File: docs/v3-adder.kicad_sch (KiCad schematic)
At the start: 101 parts, among them J1 Thonkiconn, J2 Thonkiconn, J3 Thonkiconn, J4 Thonkiconn, J5 Thonkiconn, J6 Thonkiconn, J7 Thonkiconn, J8 Thonkiconn, P1 Eurorack 2x5, SW1A SUBMINI ON-OFF-ON, SW1B SUBMINI ON-ON, SW2A SUBMINI ON-OFF-ON, SW2B SUBMINI ON-ON-ON, SW3A SUBMINI ON-OFF-ON, SW3B SUBMINI ON-ON-ON, SW4A SUBMINI ON-OFF-ON, SW4B SUBMINI ON-ON-ON, U1 OPA4196, U2 OPA4196, U3 OPA4196, U4 L78L05, U5 L79L05

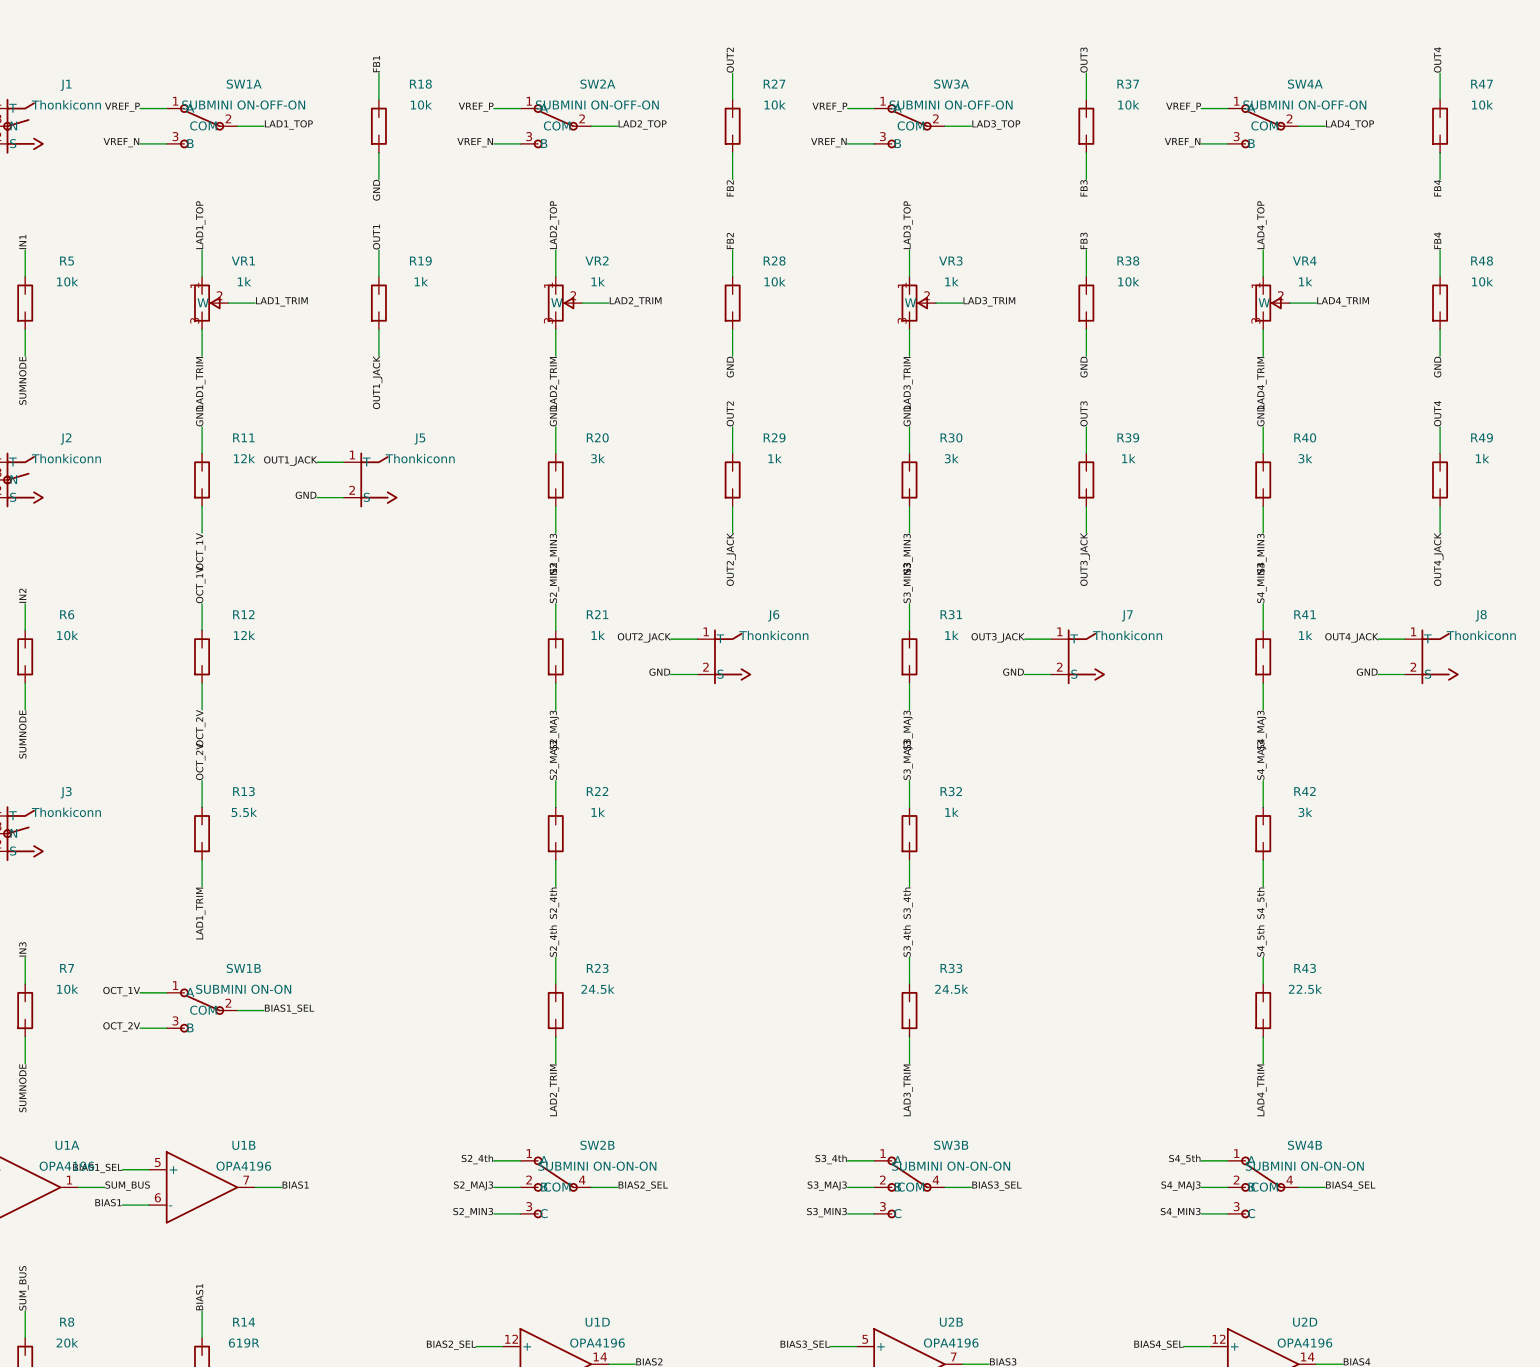
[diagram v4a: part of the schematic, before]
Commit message: Schematic: wire the real Taiway switches, cross-check against the panel
Part is Taiway 200-MDP6-T1B1M2QE. Datasheet fetched and read: series 200
subminiature, pins 1-2-3 pole A with 2 common, 4-5-6 pole B with 5 common,
B1 bushing 10-48 UNS Ø4.80 with a recommended Ø4.95 panel hole - so the panel's
Ø5.0 holes are right, though it does not cut the optional 4.55 anti-rotation
flat.

The selector was drawn as an ideal 4-pin 1P3T, which no such part is. It is now
a real 6-pin DPDT with the poles cascaded: pole A's common is the output, one
of its throws is a tap outright, the other feeds pole B's common, and pole B
picks between the remaining two. Tying the commons instead would short two
ladder taps in every position.

MDP-6 is not in Taiway's catalogue - the sheet documents MDP-1..MDP-5 and says
custom configurations are by request - so its contact sequence is unpublished
and two are possible. ONONON_VARIANT selects between them, defaulting to 1,
with the meter check documented. It changes only which of pins 1/3 carries a
tap and which links to pole B.

Wiring the switch properly exposed a cross-artifact bug: the schematic put the
4th on the up throw while the panel silkscreens MAJ there. That would have
shipped a module whose front lied about its own switches. Throws are now named
explicitly rather than positionally, and check_panel_agreement() imports the
panel generator and asserts that every printed label matches the tap it wires,
and that each group drives the output it claims. Verified against a swap.

BOM now carries real part numbers: 4x 200-MSP3 polarity, 1x 200-MSP1 octave
magnitude, 3x 200-MDP6 quality.

ERC still 0 errors, 23 footprint warnings on the custom parts.

Co-Authored-By: Claude Opus 5 <noreply@anthropic.com>
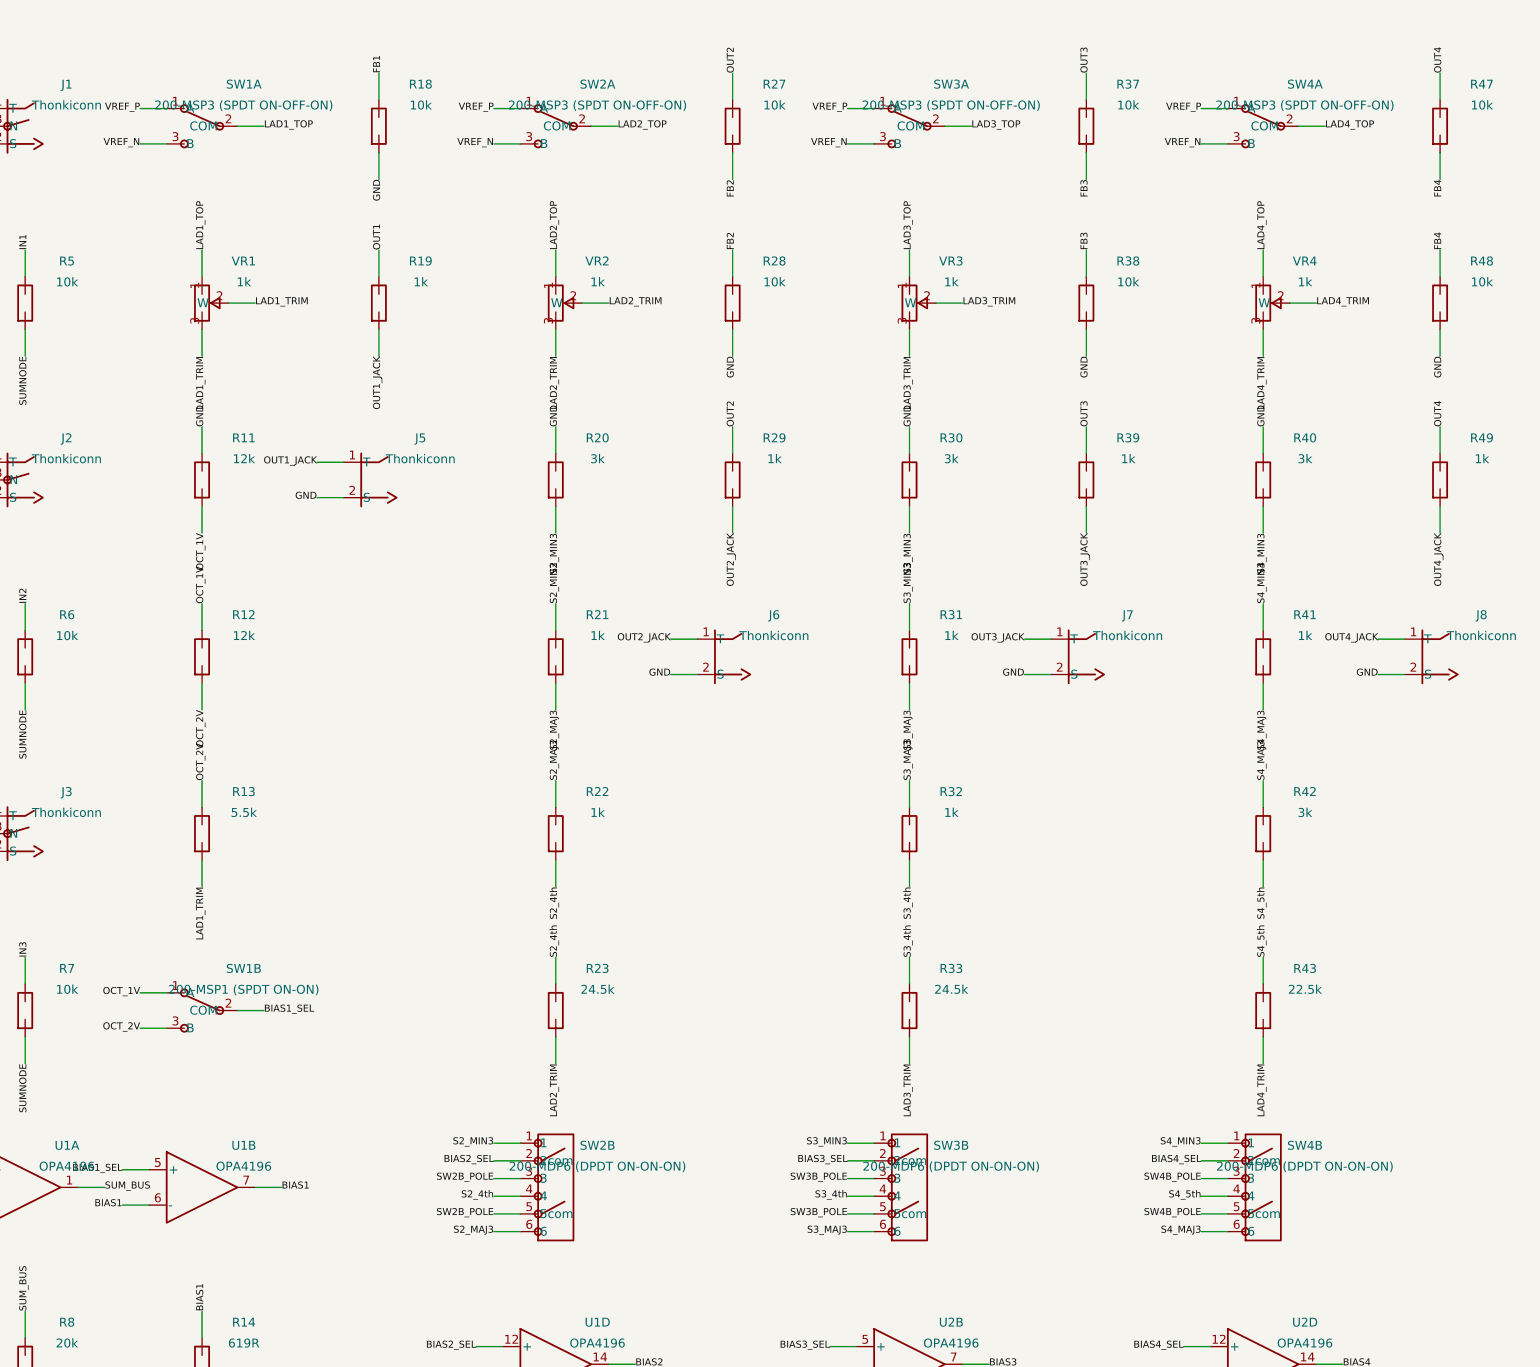
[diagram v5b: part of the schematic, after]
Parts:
- removed C20: 330pF, Capacitor_SMD:C_0805_2012Metric, symbol adder:C
- removed R44: 619R, Resistor_SMD:R_0805_2012Metric, symbol adder:R
- removed R47, R48: 10k, Resistor_SMD:R_0805_2012Metric, symbol adder:R
- removed SW3A, SW4A: SUBMINI ON-OFF-ON, SUBMINI_TOGGLE, symbol adder:SW_ONOFFON
- removed SW3B, SW4B: SUBMINI ON-ON-ON, SUBMINI_TOGGLE, symbol adder:SW_1P3T
- removed unit 2 of U2
- removed unit 3 of U2
- added J8: Thonkiconn, THONKICONN-TIGHT, symbol adder:JACK
- added R34: 619R, Resistor_SMD:R_0805_2012Metric, symbol adder:R
- added R37, R46: 10k, Resistor_SMD:R_0805_2012Metric, symbol adder:R
- added R40: 3k, Resistor_SMD:R_0805_2012Metric, symbol adder:R
- added R49: 1k, Resistor_SMD:R_0805_2012Metric, symbol adder:R
- added SW3A: 200-MSP3 (SPDT ON-OFF-ON), TAIWAY_200_SP_M2, symbol adder:SW_ONON
- added SW3B, SW4B: 200-MDP6 (DPDT ON-ON-ON), TAIWAY_200_DP_M2, symbol adder:SW_DPDT
- added unit 1 of U3
- C20: renamed from R46; value 10k -> 330pF; footprint Resistor_SMD:R_0805_2012Metric -> Capacitor_SMD:C_0805_2012Metric; symbol adder:R -> adder:C
- R44: renamed from R45; value 10k -> 619R
- R45: renamed from U3; value OPA4196 -> 10k; footprint Package_SO:SOIC-14_3.9x8.7mm_P1.27mm -> Resistor_SMD:R_0805_2012Metric; symbol adder:OPA4196 -> adder:R
- R47: renamed from R49; value 1k -> 10k
- R48: renamed from J8; value Thonkiconn -> 10k; footprint THONKICONN-TIGHT -> Resistor_SMD:R_0805_2012Metric; symbol adder:JACK -> adder:R
- SW1A, SW2A: value SUBMINI ON-OFF-ON -> 200-MSP3 (SPDT ON-OFF-ON); footprint SUBMINI_TOGGLE -> TAIWAY_200_SP_M2; symbol adder:SW_ONOFFON -> adder:SW_ONON
- SW1B: value SUBMINI ON-ON -> 200-MSP1 (SPDT ON-ON); footprint SUBMINI_TOGGLE -> TAIWAY_200_SP_M2; symbol adder:SW_ONOFFON -> adder:SW_ONON
- SW2B: value SUBMINI ON-ON-ON -> 200-MDP6 (DPDT ON-ON-ON); footprint SUBMINI_TOGGLE -> TAIWAY_200_DP_M2; symbol adder:SW_1P3T -> adder:SW_DPDT
- SW4A: renamed from VR4; value 1k -> 200-MSP3 (SPDT ON-OFF-ON); footprint PV36W-MULTITURN-TRIMMER -> TAIWAY_200_SP_M2; symbol adder:POT -> adder:SW_ONON
- U2: renamed from R34; value 619R -> OPA4196; footprint Resistor_SMD:R_0805_2012Metric -> Package_SO:SOIC-14_3.9x8.7mm_P1.27mm; symbol adder:R -> adder:OPA4196
- U2: renamed from R37; value 10k -> OPA4196; footprint Resistor_SMD:R_0805_2012Metric -> Package_SO:SOIC-14_3.9x8.7mm_P1.27mm; symbol adder:R -> adder:OPA4196
- VR4: renamed from R40; value 3k -> 1k; footprint Resistor_SMD:R_0805_2012Metric -> PV36W-MULTITURN-TRIMMER; symbol adder:R -> adder:POT
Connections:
- net BIAS2_SEL: now also SW2B.2 (2com); no longer SW2B.4 (COM)
- net BIAS3: now also U2.6 (-), U2.7, R34.1; no longer U2.1
- net BIAS3_SEL: now also U2.5 (+), SW3B.2 (2com)
- net BIAS3_SNUB: now also R34.2; no longer U2.2
- net BIAS4: now also R44.1, R46.1; no longer C20.1
- net BIAS4_SEL: now also SW4B.2 (2com)
- net BIAS4_SNUB: now also C20.1, R44.2
- net FB3: now also U2.9 (-), R37.2; no longer U2.2
- net FB4: now also R47.2, R48.1, U3.2 (-); no longer R45.2 (-)
- net GND: now also C20.2, J8.2 (S), R40.1; no longer VR4.1
- net LAD3_TOP: now also SW3A.2 (COM)
- net LAD4_TOP: now also SW4A.2 (COM), VR4.1; no longer SW4A.1
- net LAD4_TRIM: now also VR4.2 (W), VR4.3; no longer SW4A.2 (W), SW4A.3
- net OUT3: now also R45.1, U2.8, R37.1; no longer R44.1, U2.1
- net OUT4: now also R49.1, U3.1; no longer R45.1
- net OUT4_JACK: now also J8.1 (T), R49.2; no longer R47.2, R48.1 (T)
- net S2_4th: now also SW2B.4; no longer SW2B.1 (A)
- net S2_MAJ3: now also SW2B.6; no longer SW2B.2 (B)
- net S2_MIN3: now also SW2B.1; no longer SW2B.3 (C)
- net S3_4th: now also SW3B.4
- net S3_MAJ3: now also SW3B.6
- net S3_MIN3: now also SW3B.1
- net S4_5th: now also SW4B.4
- net S4_MAJ3: now also SW4B.6
- net S4_MIN3: now also R40.2, SW4B.1; no longer VR4.2
- net SUM3: now also U2.10 (+)
- net SUM4: now also R45.2, R46.2, U3.3 (+); no longer C20.2, R44.2, R45.3 (+)
- net VREF_N: now also SW4A.3 (B), SW3A.3 (B)
- net VREF_P: now also SW4A.1 (A), SW3A.1 (A)
- new net SW2B_POLE: SW2B.3, SW2B.5 (5com)
- new net SW3B_POLE: SW3B.3, SW3B.5 (5com)
- new net SW4B_POLE: SW4B.3, SW4B.5 (5com)
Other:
- moved on the sheet: R44, R47

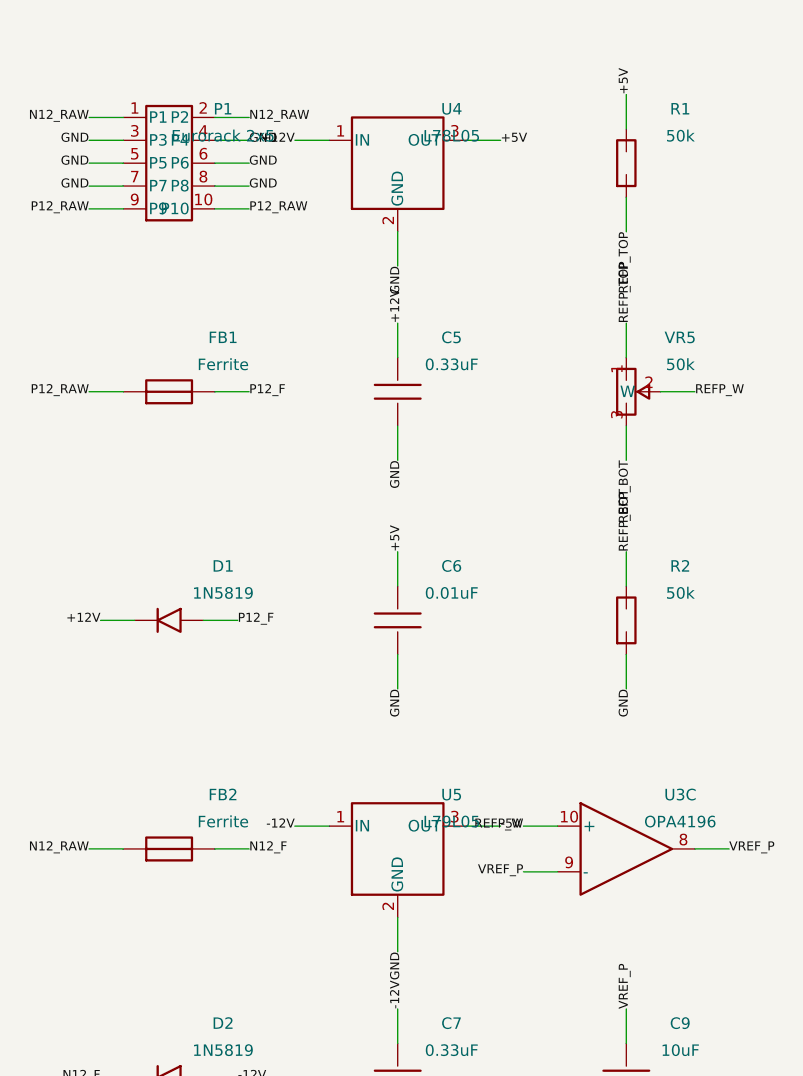
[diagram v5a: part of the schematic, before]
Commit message: Fix both regulator pinouts; wire them by function, not pin number
Asked whether U5 pin 3 is -5V. It is, and that one happens to be right - but
checking it against the v2.2 schematic showed the other five regulator pins
were wrong.

The 78L05 and 79L05 do not share a pinout in TO-92:

  78L05   3 = IN   2 = GND   1 = OUT
  79L05   2 = IN   1 = GND   3 = OUT

I had one generic REG symbol numbered 1=IN, 2=GND, 3=OUT and used it for both,
so U4 had +12V on its output pin and +5V on its input, and U5 had -12V on its
ground pin and ground on its input. Only U5 pin 3 landed correctly, which is
the pin that got asked about.

Now two symbols carrying the real numbering, and add_reg() looks the numbers up
from the symbol's own pin names, so callers name IN/OUT/GND and cannot get the
order backwards. check_regulators() asserts each pin carries its intended rail;
swapping U5 pins 1 and 2 reproduces the old bug and is caught.

Worth noting ERC could not see any of this - every pin was connected to a real
net and every net had several pins. It was only wrong against the part.

Co-Authored-By: Claude Opus 5 <noreply@anthropic.com>
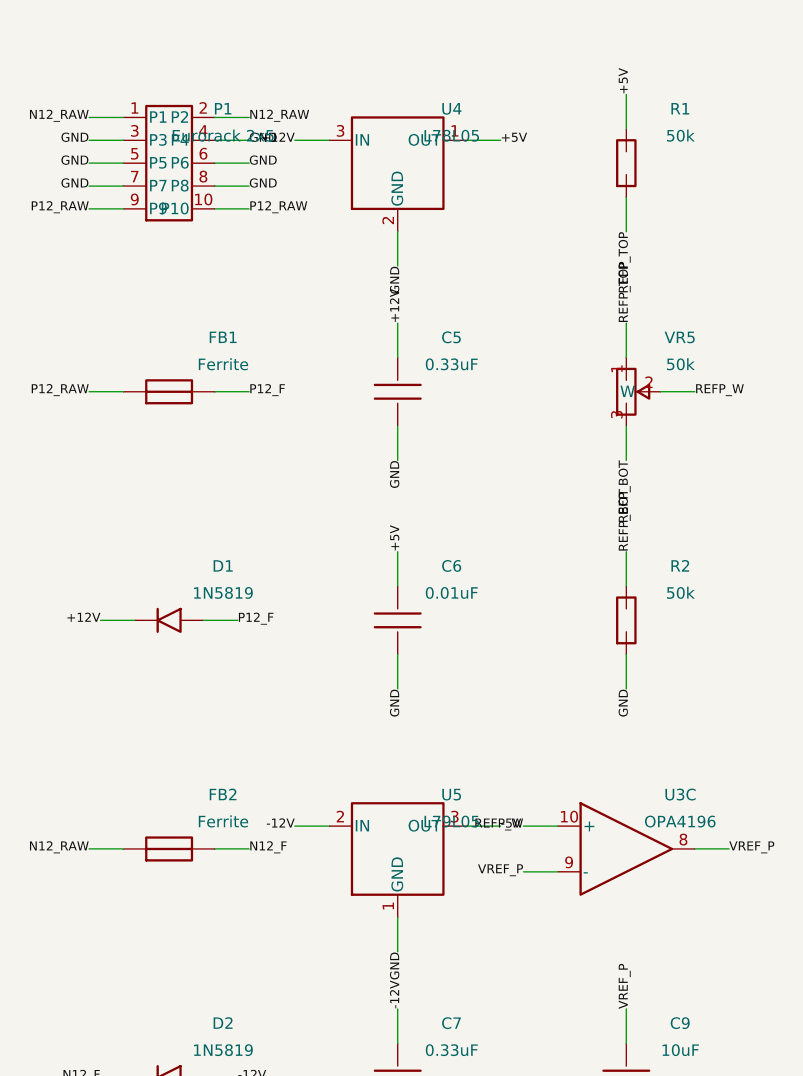
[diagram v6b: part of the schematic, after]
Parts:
- U4: symbol adder:REG -> adder:REG_POS
- U5: symbol adder:REG -> adder:REG_NEG
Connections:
- net +12V: now also U4.3 (IN); no longer U4.1 (IN)
- net +5V: now also U4.1 (OUT); no longer U4.3 (OUT)
- net -12V: now also U5.2 (IN); no longer U5.1 (IN)
- net GND: now also U5.1 (GND); no longer U5.2 (GND)
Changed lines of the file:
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@@
     )
   )
-  (symbol (lib_id "adder:REG") (at 63.5 38.1 0) (unit 1) (in_bom yes) (on_board yes) (dnp no)
+  (symbol (lib_id "adder:REG_POS") (at 63.5 38.1 0) (unit 1) (in_bom yes) (on_board yes) (dnp no)
     (property "Reference" "U4" (at 69.5 32.1 0) (effects (font (size 1.27 1.27))))
     (property "Value" "L78L05" (at 69.5 35.1 0) (effects (font (size 1.27 1.27))))
     (property "Footprint" "Package_TO_SOT_THT:TO-92_Inline" (at 63.5 38.1 0) (effects (font (size 1.27 1.27)) hide))
     (property "Datasheet" "~" (at 63.5 38.1 0) (effects (font (size 1.27 1.27)) hide))
+    (pin "3")
+    (pin "2")
     (pin "1")
-    (pin "2")
-    (pin "3")
     (instances
       (project "v3-adder"
@@
     )
   )
-  (symbol (lib_id "adder:REG") (at 63.5 114.29999999999998 0) (unit 1) (in_bom yes) (on_board yes) (dnp no)
+  (symbol (lib_id "adder:REG_NEG") (at 63.5 114.29999999999998 0) (unit 1) (in_bom yes) (on_board yes) (dnp no)
     (property "Reference" "U5" (at 69.5 108.29999999999998 0) (effects (font (size 1.27 1.27))))
     (property "Value" "L79L05" (at 69.5 111.29999999999998 0) (effects (font (size 1.27 1.27))))
     (property "Footprint" "Package_TO_SOT_THT:TO-92_Inline" (at 63.5 114.29999999999998 0) (effects (font (size 1.27 1.27)) hide))
     (property "Datasheet" "~" (at 63.5 114.29999999999998 0) (effects (font (size 1.27 1.27)) hide))
+    (pin "2")
     (pin "1")
-    (pin "2")
     (pin "3")
     (instances
